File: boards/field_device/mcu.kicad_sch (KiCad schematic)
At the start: 10 parts, among them J1 Conn_01x05_Pin, U2 STM32C051F6P6

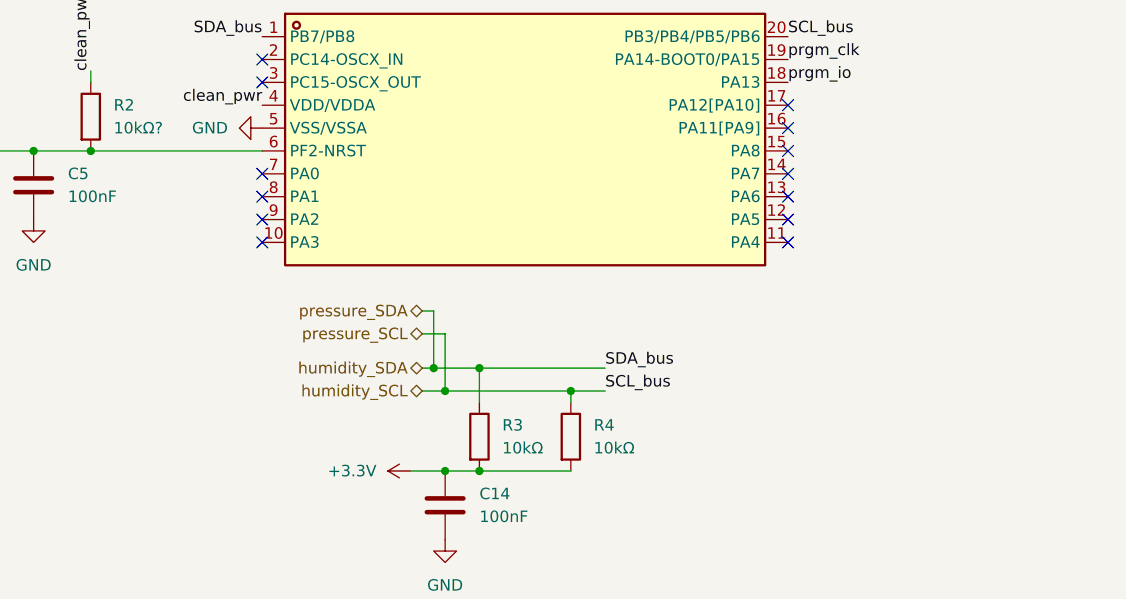
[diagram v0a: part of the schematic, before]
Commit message: connected lora to mcu
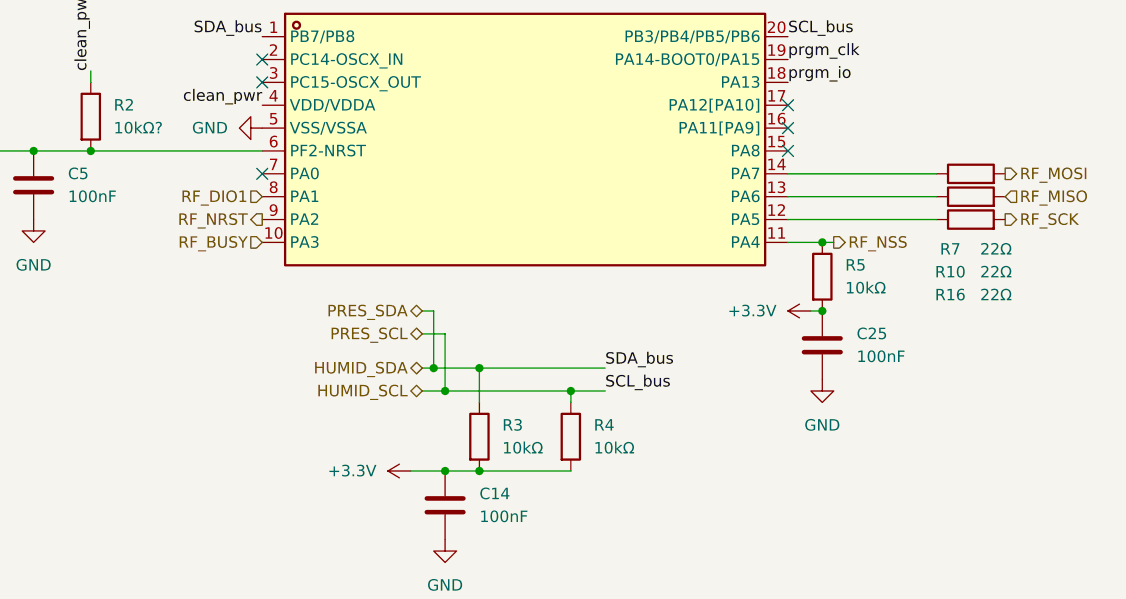
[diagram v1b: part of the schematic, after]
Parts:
- added C25: 100nF, symbol Device:C
- added R10, R16, R7: 22Ω, symbol Device:R
- added R5: 10kΩ, symbol Device:R
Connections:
- net +3.3V: now also C25.1, R5.2
- net GND: now also C25.2
- net RF_BUSY: now reaches U2.10 (PA3)
- net RF_NSS: now reaches U2.11 (PA4)
- net RF_NSS: now also R5.1
- net at U2.12 (PA5): now also R16.1
- net at U2.13 (PA6): now also R10.1
- net at U2.14 (PA7): now also R7.1
- net RF_DIO1: now reaches U2.8 (PA1)
- net RF_NRST: now reaches U2.9 (PA2)
- net humidity_SCL renamed HUMID_SCL
- net humidity_SDA renamed HUMID_SDA
- new net RF_MISO: R10.2
- new net RF_MOSI: R7.2
- new net RF_SCK: R16.2
- no-connect marks 13 -> 6

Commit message: fun
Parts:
- added SW1: SW_SPST, UnEasy-LCSC:KEY-SMD_L3.9-W3.0-LS5.0-EH, symbol Switch:SW_SPST
- C6: renamed from C14; footprint (none) -> Capacitor_SMD:C_0603_1608Metric
- C7: renamed from C25; footprint (none) -> Capacitor_SMD:C_0603_1608Metric
- R3, R4: footprint Package_DIP:DIP-8_W7.62mm -> Resistor_SMD:R_0603_1608Metric
- R5: footprint (none) -> Resistor_SMD:R_0603_1608Metric
- R6: renamed from R7; footprint (none) -> Resistor_SMD:R_0603_1608Metric
- R7: renamed from R10; footprint (none) -> Resistor_SMD:R_0603_1608Metric
- R8: renamed from R16; footprint (none) -> Resistor_SMD:R_0603_1608Metric
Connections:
- net GND: now also SW1.1 (A)
- net prgm_nrst: now also SW1.2 (B)
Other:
- moved on the sheet: C7

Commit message: actual shit in a kettle (added uart pins)
WRITING REGISTERS IS PAIN!!!!!!!!!
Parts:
- added J2: Conn_01x02_Pin, Connector_PinHeader_1.00mm:PinHeader_1x02_P1.00mm_Vertical, symbol Connector:Conn_01x02_Pin
- added R17, R18: 1kΩ, symbol Device:R
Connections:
- net at U2.16 (PA11[PA9]): now also R18.1
- net at U2.17 (PA12[PA10]): now also R17.1
- new net LOG_MCU_RX_DEBUGGER_TX: J2.1 (Pin_1), R17.2
- new net LOG_MCU_TX_DEBUGGER_RX: J2.2 (Pin_2), R18.2
- no-connect marks 6 -> 4

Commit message: reorganized mcu
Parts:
- removed C2: 4.7uF, Capacitor_SMD:C_0603_1608Metric, symbol Device:C
- removed C3, C4: 100nF, Capacitor_SMD:C_0603_1608Metric, symbol Device:C
- removed U2: STM32C051F6P6, LCSC downloads:TSSOP-20_L6.5-W4.4-P0.65-LS6.4-BL, symbol lcsc downloads:STM32C051F6P6
- added C26: 100n, Capacitor_SMD:C_0603_1608Metric, symbol Device:C
- added U7: STM32C011F6Px, Package_SO:TSSOP-20_4.4x6.5mm_P0.65mm, symbol MCU_ST_STM32C0:STM32C011F6Px
- C5, C7: value 100nF -> 100n
- C6: value 100nF -> 4.7u
- R17, R18: value 1kΩ -> 1k
- R2: value 10kΩ? -> 10k?
- R3, R4, R5: value 10kΩ -> 10k
- R6, R7, R8: value 22Ω -> 22R
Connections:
- net +3.3V: now also C26.1, U7.4 (VDD)
- net GND: now also C26.2, U7.5 (VSS)
- net HUMID_SCL: now also U7.20 (PB6)
- net HUMID_SDA: now also U7.1 (PB7)
- net LOG_MCU_RX_DEBUGGER_TX: now also J2.2 (Pin_2); no longer J2.1 (Pin_1)
- net LOG_MCU_TX_DEBUGGER_RX: now also J2.1 (Pin_1); no longer J2.2 (Pin_2)
- net RF_BUSY: now also U7.10 (PA3)
- net RF_DIO1: now also U7.8 (PA1)
- net RF_MISO: now also R7.1, U7.13 (PA6)
- net RF_MOSI: now also R6.1, U7.14 (PA7)
- net RF_NRST: now also U7.9 (PA2)
- net RF_NSS: now also U7.11 (PA4)
- net RF_SCK: now also R8.1, U7.12 (PA5)
- net LOG_MCU_TX: now reaches R18.1
- net LOG_MCU_TX: now also U7.16 (PA9/PA11)
- net LOG_MCU_RX: now reaches R17.1
- net LOG_MCU_RX: now also U7.17 (PA10/PA12)
- net prgm_clk renamed SWDCLK
- net SWDCLK: now also U7.19 (PA14)
- net prgm_io renamed SWDIO
- net SWDIO: now also U7.18 (PA13)
- net prgm_nrst renamed NRST
- net NRST: now also U7.6 (PF2)
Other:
- note removed: "programming pins"
- moved on the sheet: C5, J1, J2, R17, R18, R2, R3, R4, R5, R6, R7, R8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

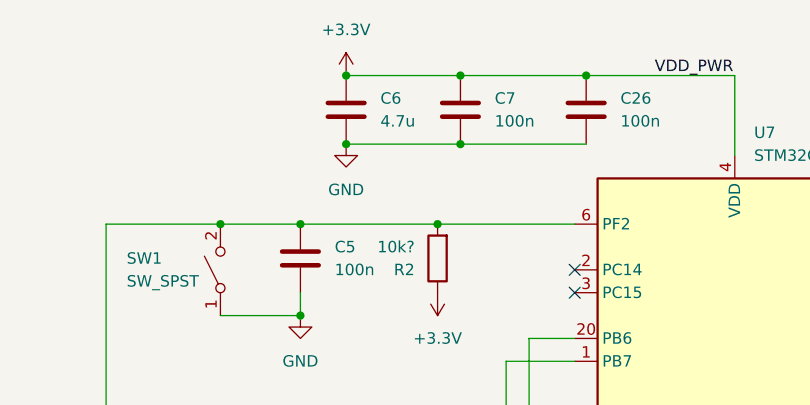
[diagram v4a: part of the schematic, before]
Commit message: reorganized regulator
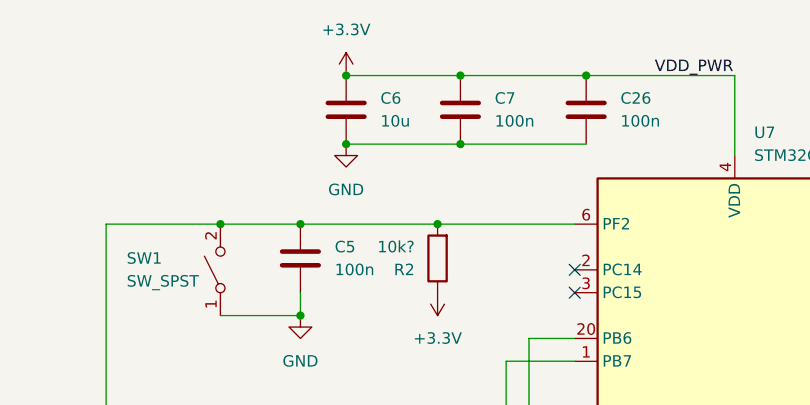
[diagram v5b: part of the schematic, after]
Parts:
- C6: value 4.7u -> 10u
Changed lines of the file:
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@@
 			)
 		)
-		(property "Value" "4.7u"
+		(property "Value" "10u"
 			(at 87.63 33.0199 0)
 			(show_name no)

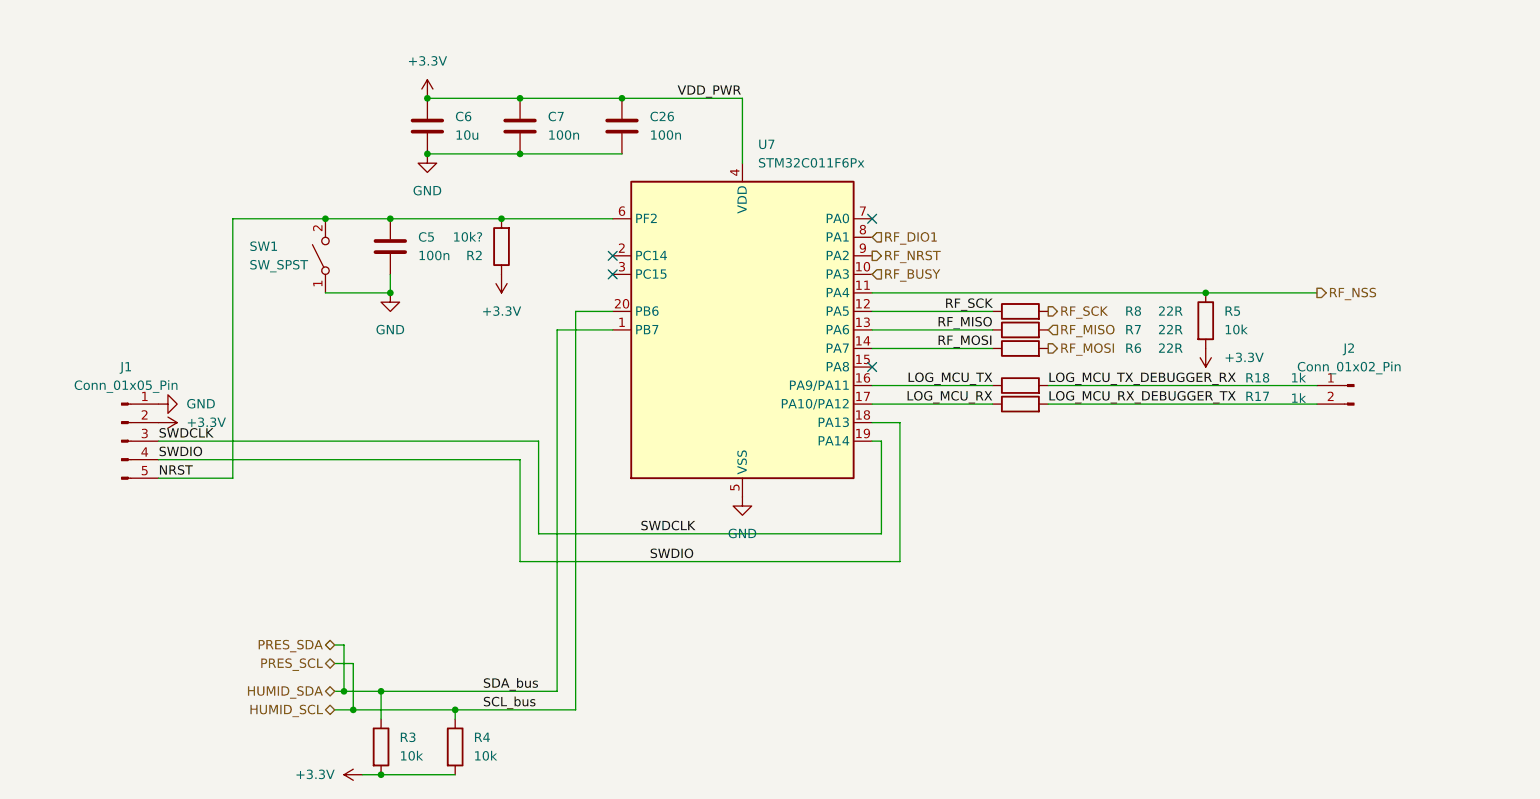
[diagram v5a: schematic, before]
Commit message: added satus leds
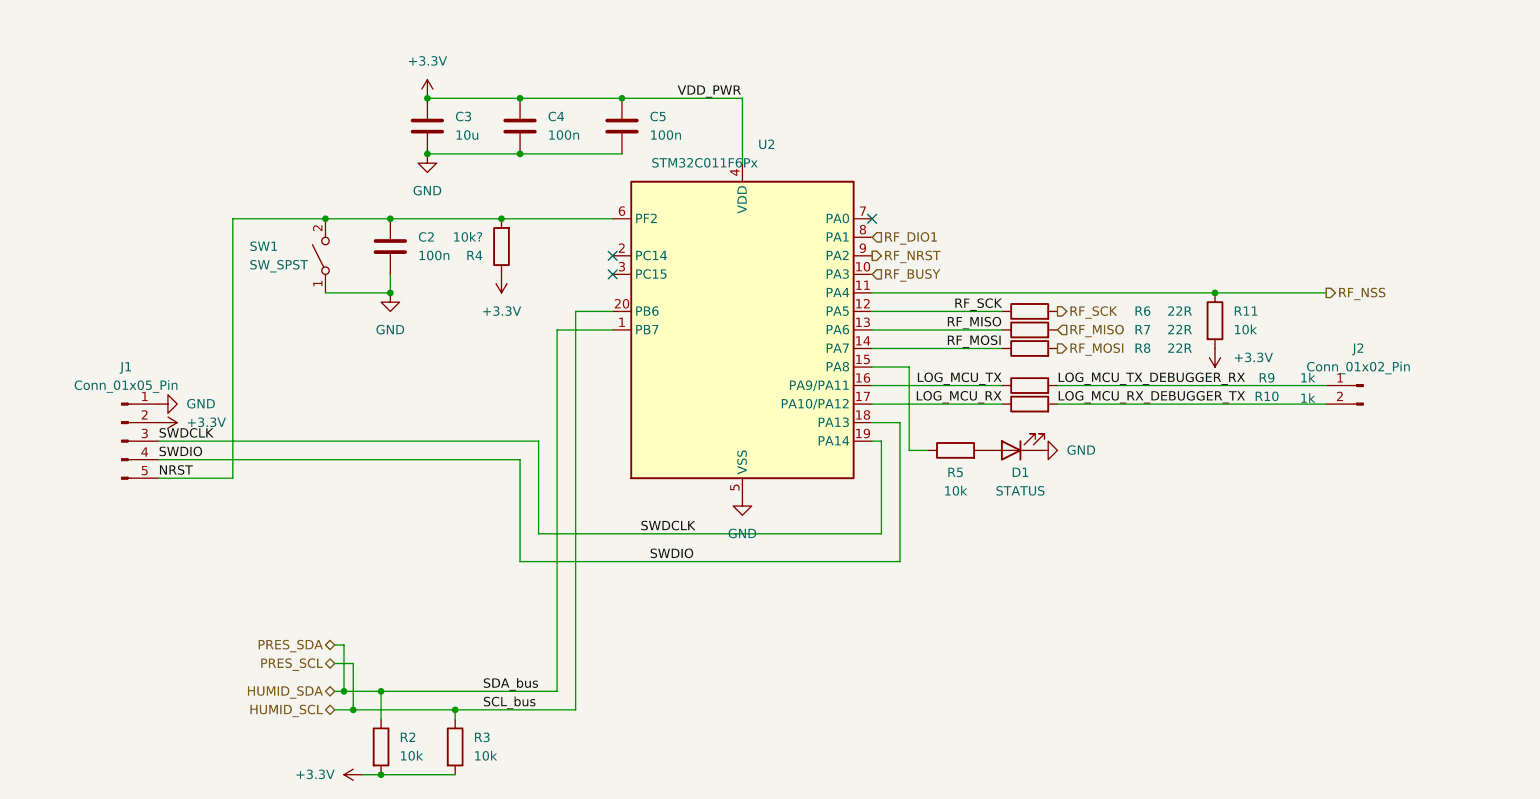
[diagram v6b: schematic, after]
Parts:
- added D1: STATUS, symbol Device:LED
- added R5: 10k, symbol Device:R
- renumbered C5 to C2, C6 to C3, C7 to C4, C26 to C5, R17 to R10, R5 to R11, R3 to R2, R4 to R3, R2 to R4, R8 to R6, R6 to R8, R18 to R9, U7 to U2
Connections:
- net GND: now also D1.1 (K)
- net at U2.15 (PA8): now also R5.1
- new net: D1.2 (A), R5.2
- no-connect marks 4 -> 3
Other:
- moved on the sheet: J2, R10, R11, R6, R7, R8, R9

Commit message: i guess made schematic more readable?
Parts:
- C2, C4, C5: footprint Capacitor_SMD:C_0603_1608Metric -> Capacitor_SMD:C_0603_1608Metric_Pad1.08x0.95mm_HandSolder
- C3: footprint Capacitor_SMD:C_0603_1608Metric -> Capacitor_SMD:C_0805_2012Metric_Pad1.18x1.45mm_HandSolder
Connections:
- net STATUS_LED: now reaches R5.1, U2.15 (PA8)
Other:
- moved on the sheet: D1, R5
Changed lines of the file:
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@@
 	(wire
 		(pts
-			(xy 149.86 76.2) (xy 152.4 76.2)
+			(xy 149.86 76.2) (xy 170.18 76.2)
 		)
 		(stroke
@@
 			(width 0)
 			(type default)
+		)
+	)
+	(label "STATUS_LED"
+		(at 162.56 76.2 180)
+		(effects
+			(font
+				(size 1.27 1.27)
+			)
+			(justify right bottom)
 		)
 	)
@@
 			)
 		)
-		(property "Footprint" "Capacitor_SMD:C_0603_1608Metric"
+		(property "Footprint" "Capacitor_SMD:C_0603_1608Metric_Pad1.08x0.95mm_HandSolder"
 			(at 97.4852 35.56 0)
 			(hide yes)
@@
 	(symbol
 		(lib_id "power:GND")
-		(at 167.64 76.2 90)
+		(at 185.42 76.2 90)
 		(unit 1)
 		(body_style 1)
@@
 		(fields_autoplaced yes)
 		(property "Reference" "#PWR012"
-			(at 173.99 76.2 0)
+			(at 191.77 76.2 0)
 			(hide yes)
 			(show_name no)
@@
 		)
 		(property "Value" "GND"
-			(at 171.45 76.1999 90)
+			(at 189.23 76.1999 90)
 			(show_name no)
 			(do_not_autoplace no)
@@
 		)
 		(property "Footprint" ""
-			(at 167.64 76.2 0)
-			(hide yes)
-			(show_name no)
-			(do_not_autoplace no)
-			(effects
-				(font
-					(size 1.27 1.27)
-				)
-			)
-		)
-		(property "Datasheet" ""
-			(at 167.64 76.2 0)
+			(at 185.42 76.2 0)
+			(hide yes)
+			(show_name no)
+			(do_not_autoplace no)
+			(effects
+				(font
+					(size 1.27 1.27)
+				)
+			)
+		)
+		(property "Datasheet" ""
+			(at 185.42 76.2 0)
 			(hide yes)
 			(show_name no)
@@
 		)
 		(property "Description" "Power symbol creates a global label with name \"GND\" , ground"
-			(at 167.64 76.2 0)
+			(at 185.42 76.2 0)
 			(hide yes)
 			(show_name no)
@@
 			)
 		)
-		(property "Footprint" "Capacitor_SMD:C_0603_1608Metric"
+		(property "Footprint" "Capacitor_SMD:C_0603_1608Metric_Pad1.08x0.95mm_HandSolder"
 			(at 79.7052 52.07 0)
 			(hide yes)
@@
 			)
 		)
-		(property "Footprint" "Capacitor_SMD:C_0603_1608Metric"
+		(property "Footprint" "Capacitor_SMD:C_0603_1608Metric_Pad1.08x0.95mm_HandSolder"
 			(at 111.4552 35.56 0)
 			(hide yes)
@@
 			)
 		)
-		(property "Footprint" "Capacitor_SMD:C_0603_1608Metric"
+		(property "Footprint" "Capacitor_SMD:C_0805_2012Metric_Pad1.18x1.45mm_HandSolder"
 			(at 84.7852 35.56 0)
 			(hide yes)
@@
 	(symbol
 		(lib_id "Device:LED")
-		(at 163.83 76.2 180)
+		(at 181.61 76.2 180)
 		(unit 1)
 		(body_style 1)
@@
 		(dnp no)
 		(property "Reference" "D1"
-			(at 165.1 79.248 0)
+			(at 182.88 79.248 0)
 			(show_name no)
 			(do_not_autoplace no)
@@
 		)
 		(property "Value" "STATUS"
-			(at 165.1 81.788 0)
+			(at 182.88 81.788 0)
 			(show_name no)
 			(do_not_autoplace no)
@@
 		)
 		(property "Footprint" ""
-			(at 163.83 76.2 0)
-			(hide yes)
-			(show_name no)
-			(do_not_autoplace no)
-			(effects
-				(font
-					(size 1.27 1.27)
-				)
-			)
-		)
-		(property "Datasheet" ""
-			(at 163.83 76.2 0)
+			(at 181.61 76.2 0)
+			(hide yes)
+			(show_name no)
+			(do_not_autoplace no)
+			(effects
+				(font
+					(size 1.27 1.27)
+				)
+			)
+		)
+		(property "Datasheet" ""
+			(at 181.61 76.2 0)
 			(hide yes)
 			(show_name no)
@@
 		)
 		(property "Description" "Light emitting diode"
-			(at 163.83 76.2 0)
+			(at 181.61 76.2 0)
 			(hide yes)
 			(show_name no)
@@
 		)
 		(property "Sim.Pins" "1=K 2=A"
-			(at 163.83 76.2 0)
+			(at 181.61 76.2 0)
 			(hide yes)
 			(show_name no)
@@
 	(symbol
 		(lib_id "Device:R")
-		(at 156.21 76.2 90)
+		(at 173.99 76.2 90)
 		(unit 1)
 		(body_style 1)
@@
 		(dnp no)
 		(property "Reference" "R5"
-			(at 156.21 79.248 90)
+			(at 173.99 79.248 90)
 			(show_name no)
 			(do_not_autoplace no)
@@
 		)
 		(property "Value" "10k"
-			(at 156.21 81.788 90)
+			(at 173.99 81.788 90)
 			(show_name no)
 			(do_not_autoplace no)
@@
 		)
 		(property "Footprint" ""
-			(at 156.21 77.978 90)
-			(hide yes)
-			(show_name no)
-			(do_not_autoplace no)
-			(effects
-				(font
-					(size 1.27 1.27)
-				)
-			)
-		)
-		(property "Datasheet" ""
-			(at 156.21 76.2 0)
+			(at 173.99 77.978 90)
+			(hide yes)
+			(show_name no)
+			(do_not_autoplace no)
+			(effects
+				(font
+					(size 1.27 1.27)
+				)
+			)
+		)
+		(property "Datasheet" ""
+			(at 173.99 76.2 0)
 			(hide yes)
 			(show_name no)
@@
 		)
 		(property "Description" "Resistor"
-			(at 156.21 76.2 0)
-			(hide yes)
-			(show_name no)
+			(at 173.99 76.2 0)
+			(hide yes)
+			(show_name no)

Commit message: assigned better footprints
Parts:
- D1: footprint (none) -> LED_SMD:LED_0603_1608Metric_Pad1.05x0.95mm_HandSolder
- R10: renamed from R5; footprint (none) -> Resistor_SMD:R_0402_1005Metric_Pad0.72x0.64mm_HandSolder
- R2, R3, R4: footprint Resistor_SMD:R_0603_1608Metric -> Resistor_SMD:R_0402_1005Metric_Pad0.72x0.64mm_HandSolder
- R5: renamed from R6; footprint Resistor_SMD:R_0603_1608Metric -> Resistor_SMD:R_0402_1005Metric_Pad0.72x0.64mm_HandSolder
- R6: renamed from R7; footprint Resistor_SMD:R_0603_1608Metric -> Resistor_SMD:R_0402_1005Metric_Pad0.72x0.64mm_HandSolder
- R7: renamed from R8; footprint Resistor_SMD:R_0603_1608Metric -> Resistor_SMD:R_0402_1005Metric_Pad0.72x0.64mm_HandSolder
- R8: renamed from R9; footprint (none) -> Resistor_SMD:R_0402_1005Metric_Pad0.72x0.64mm_HandSolder
- R9: renamed from R10; footprint (none) -> Resistor_SMD:R_0402_1005Metric_Pad0.72x0.64mm_HandSolder
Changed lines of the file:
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@@
 		(in_pos_files yes)
 		(dnp no)
-		(property "Reference" "R7"
+		(property "Reference" "R6"
 			(at 181.864 59.69 90)
 			(show_name no)
@@
 			)
 		)
-		(property "Footprint" "Resistor_SMD:R_0603_1608Metric"
+		(property "Footprint" "Resistor_SMD:R_0402_1005Metric_Pad0.72x0.64mm_HandSolder"
 			(at 166.37 61.468 90)
 			(hide yes)
@@
 			(project "field_device"
 				(path "/99623870-118f-49fe-bbf0-fb0b890db442/441958c3-66c1-4026-b548-1512d5f01f19"
-					(reference "R7")
+					(reference "R6")
 					(unit 1)
 				)
@@
 			)
 		)
-		(property "Footprint" "Resistor_SMD:R_0603_1608Metric"
+		(property "Footprint" "Resistor_SMD:R_0402_1005Metric_Pad0.72x0.64mm_HandSolder"
 			(at 75.692 116.84 90)
 			(hide yes)
@@
 		(in_pos_files yes)
 		(dnp no)
-		(property "Reference" "R6"
+		(property "Reference" "R5"
 			(at 181.864 57.15 90)
 			(show_name no)
@@
 			)
 		)
-		(property "Footprint" "Resistor_SMD:R_0603_1608Metric"
+		(property "Footprint" "Resistor_SMD:R_0402_1005Metric_Pad0.72x0.64mm_HandSolder"
 			(at 166.37 58.928 90)
 			(hide yes)
@@
 			(project "field_device"
 				(path "/99623870-118f-49fe-bbf0-fb0b890db442/441958c3-66c1-4026-b548-1512d5f01f19"
-					(reference "R6")
+					(reference "R5")
 					(unit 1)
 				)
@@
 		(in_pos_files yes)
 		(dnp no)
-		(property "Reference" "R9"
+		(property "Reference" "R8"
 			(at 198.882 66.294 90)
 			(show_name no)
@@
 			)
 		)
-		(property "Footprint" ""
+		(property "Footprint" "Resistor_SMD:R_0402_1005Metric_Pad0.72x0.64mm_HandSolder"
 			(at 166.37 69.088 90)
 			(hide yes)
@@
 			(project "field_device"
 				(path "/99623870-118f-49fe-bbf0-fb0b890db442/441958c3-66c1-4026-b548-1512d5f01f19"
-					(reference "R9")
+					(reference "R8")
 					(unit 1)
 				)
@@
 		(in_pos_files yes)
 		(dnp no)
-		(property "Reference" "R8"
+		(property "Reference" "R7"
 			(at 181.864 62.23 90)
 			(show_name no)
@@
 			)
 		)
-		(property "Footprint" "Resistor_SMD:R_0603_1608Metric"
+		(property "Footprint" "Resistor_SMD:R_0402_1005Metric_Pad0.72x0.64mm_HandSolder"
 			(at 166.37 64.008 90)
 			(hide yes)
@@
 			(project "field_device"
 				(path "/99623870-118f-49fe-bbf0-fb0b890db442/441958c3-66c1-4026-b548-1512d5f01f19"
-					(reference "R8")
+					(reference "R7")
 					(unit 1)
 				)
@@
 			)
 		)
-		(property "Footprint" "Resistor_SMD:R_0603_1608Metric"
+		(property "Footprint" "Resistor_SMD:R_0402_1005Metric_Pad0.72x0.64mm_HandSolder"
 			(at 95.758 48.26 90)
 			(hide yes)
@@
 		(in_pos_files yes)
 		(dnp no)
-		(property "Reference" "R10"
+		(property "Reference" "R9"
 			(at 198.882 68.834 90)
 			(show_name no)
@@
 			)
 		)
-		(property "Footprint" ""
+		(property "Footprint" "Resistor_SMD:R_0402_1005Metric_Pad0.72x0.64mm_HandSolder"
 			(at 166.37 71.628 90)
 			(hide yes)
@@
 			(project "field_device"
 				(path "/99623870-118f-49fe-bbf0-fb0b890db442/441958c3-66c1-4026-b548-1512d5f01f19"
-					(reference "R10")
+					(reference "R9")
 					(unit 1)
 				)
@@
 			)
 		)
-		(property "Footprint" ""
+		(property "Footprint" "LED_SMD:LED_0603_1608Metric_Pad1.05x0.95mm_HandSolder"
 			(at 181.61 76.2 0)
 			(hide yes)
@@
 			)
 		)
-		(property "Footprint" "Resistor_SMD:R_0603_1608Metric"
+		(property "Footprint" "Resistor_SMD:R_0402_1005Metric_Pad0.72x0.64mm_HandSolder"
 			(at 85.852 116.84 90)
 			(hide yes)
@@
 		(in_pos_files yes)
 		(dnp no)
-		(property "Reference" "R5"
+		(property "Reference" "R10"
 			(at 173.99 79.248 90)
 			(show_name no)
@@
 			)
 		)
-		(property "Footprint" ""
+		(property "Footprint" "Resistor_SMD:R_0402_1005Metric_Pad0.72x0.64mm_HandSolder"
 			(at 173.99 77.978 90)
 			(hide yes)
-			(show_name no)
+			(show_name yes)
 			(do_not_autoplace no)
 			(effects
@@
 			(project "field_device"
 				(path "/99623870-118f-49fe-bbf0-fb0b890db442/441958c3-66c1-4026-b548-1512d5f01f19"
-					(reference "R5")
-					(unit 1)
-				)
+					(reference "R10")
+					(unit 1)
+				)
